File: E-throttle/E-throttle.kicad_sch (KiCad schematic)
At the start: 66 parts, among them IC1 BTS441TG, J3 Conn_01x11, J4 Conn_01x11, J5 776087-1, J9 Micro_SD_Card, Q1 NMOS, SW1 SW_Push, U1 74HC123, U2 LM317_SOT-223, U3 LM317_SOT-223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

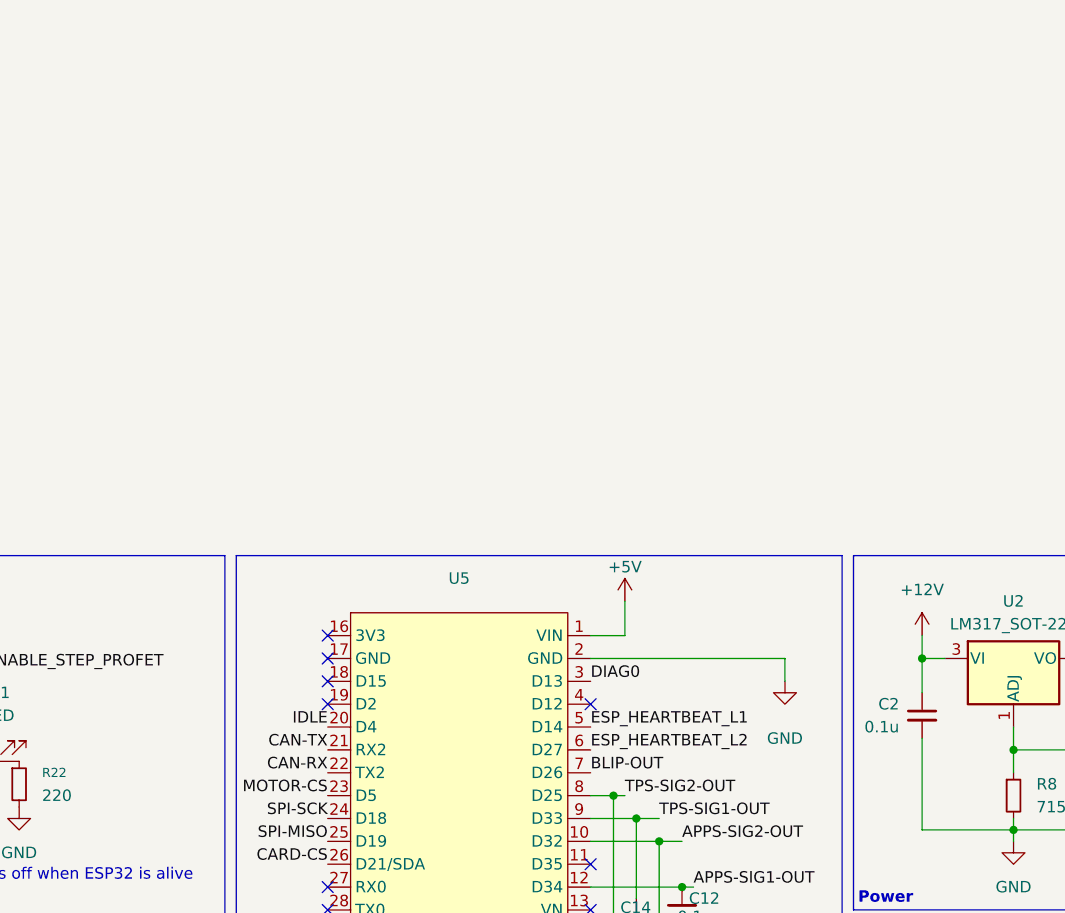
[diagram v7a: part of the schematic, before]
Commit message: Added Pin Sockets on top of ESP32 Dev Board footprint
Set ESP32 Dev board to be a ghost footprint (not included in BOM, coordinates, etc)

Added 2 1x15 female pin headers to the schematic, assigned them footprints, and aligned the precisely over the U5 pads using magnetic snapping to guarantee 25.4mm pitch
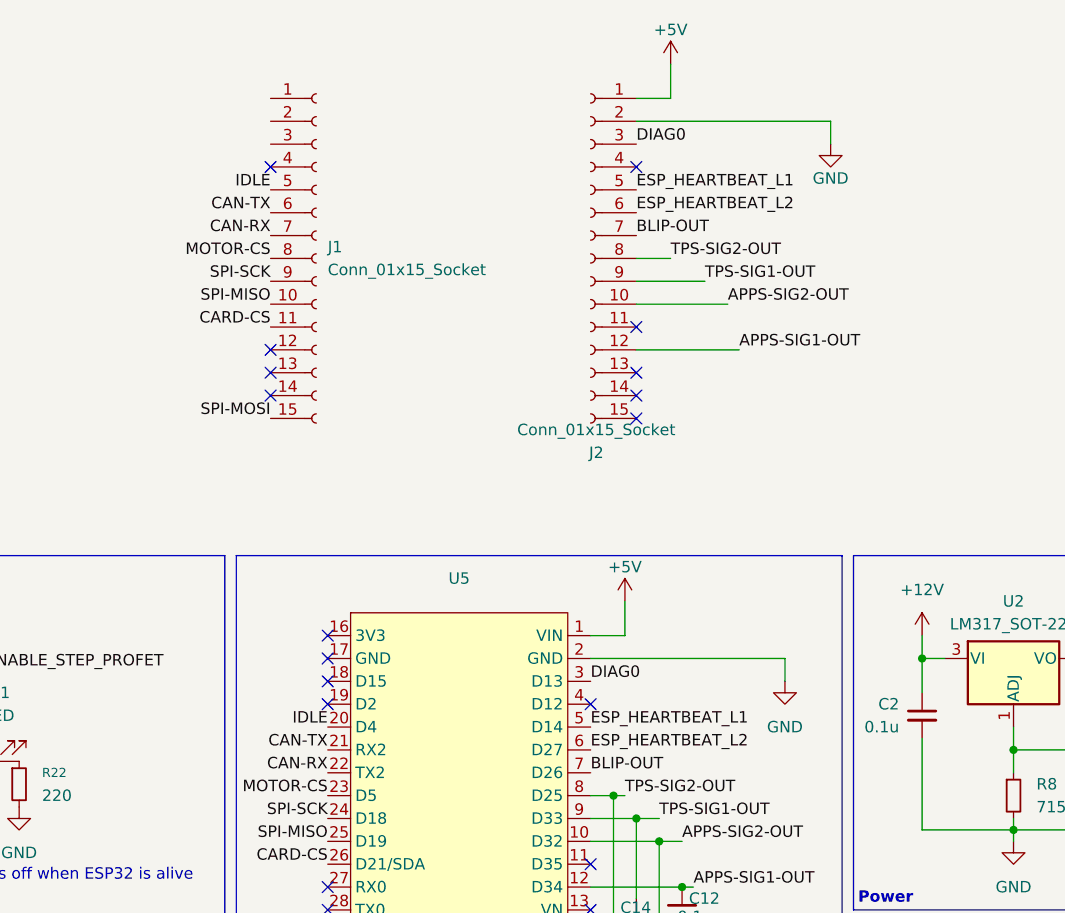
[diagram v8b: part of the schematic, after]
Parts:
- added J1, J2: Conn_01x15_Socket, Connector_PinSocket_2.54mm:PinSocket_1x15_P2.54mm_Vertical, symbol Connector:Conn_01x15_Socket
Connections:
- net +5V: now also J2.1 (Pin_1)
- net APPS-SIG1-OUT: now also J2.12 (Pin_12)
- net APPS-SIG2-OUT: now also J2.10 (Pin_10)
- net BLIP-OUT: now also J2.7 (Pin_7)
- net CAN-RX: now also J1.7 (Pin_7)
- net CAN-TX: now also J1.6 (Pin_6)
- net CARD-CS: now also J1.11 (Pin_11)
- net DIAG0: now also J2.3 (Pin_3)
- net ESP_HEARTBEAT_L1: now also J2.5 (Pin_5)
- net ESP_HEARTBEAT_L2: now also J2.6 (Pin_6)
- net GND: now also J2.2 (Pin_2)
- net IDLE: now also J1.5 (Pin_5)
- net MOTOR-CS: now also J1.8 (Pin_8)
- net SPI-MISO: now also J1.10 (Pin_10)
- net SPI-MOSI: now also J1.15 (Pin_15)
- net SPI-SCK: now also J1.9 (Pin_9)
- net TPS-SIG1-OUT: now also J2.9 (Pin_9)
- net TPS-SIG2-OUT: now also J2.8 (Pin_8)
- no-connect marks 14 -> 23
